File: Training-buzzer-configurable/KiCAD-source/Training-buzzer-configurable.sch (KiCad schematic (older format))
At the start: 16 parts, among them J1 Con, J2 DC Jack 5V, Q1 BC547B, Q2 BC547B, Q3 BC547B

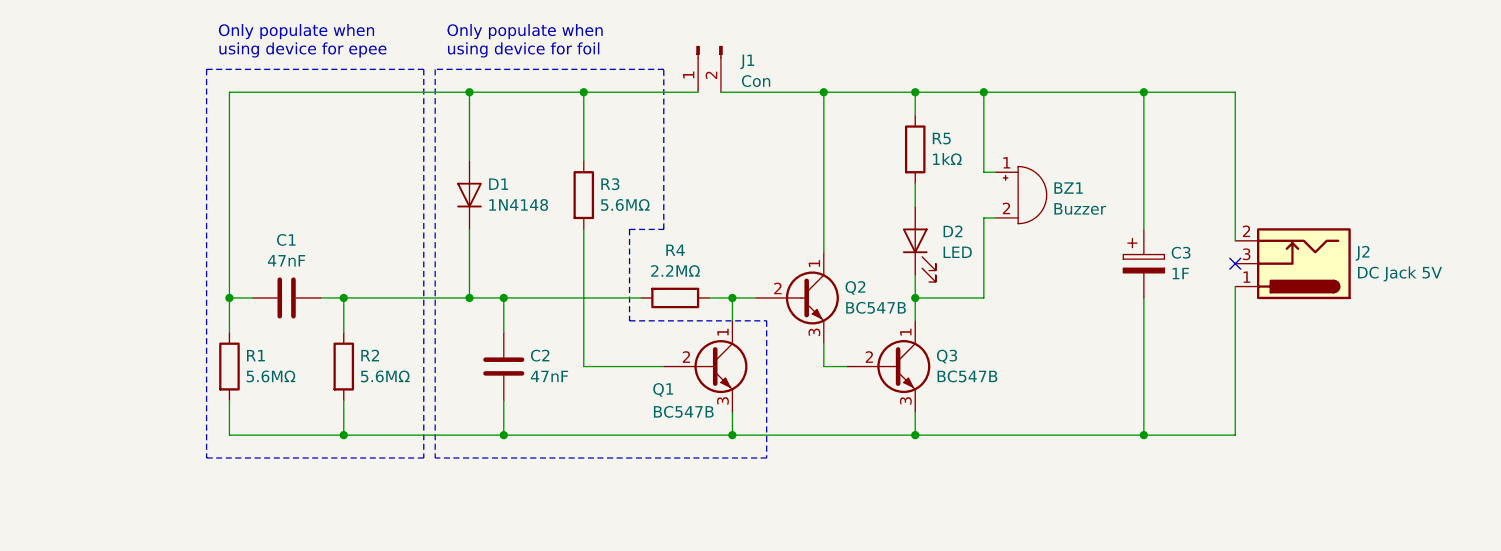
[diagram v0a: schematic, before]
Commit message: Rework circuit using NOR gates and create PCB
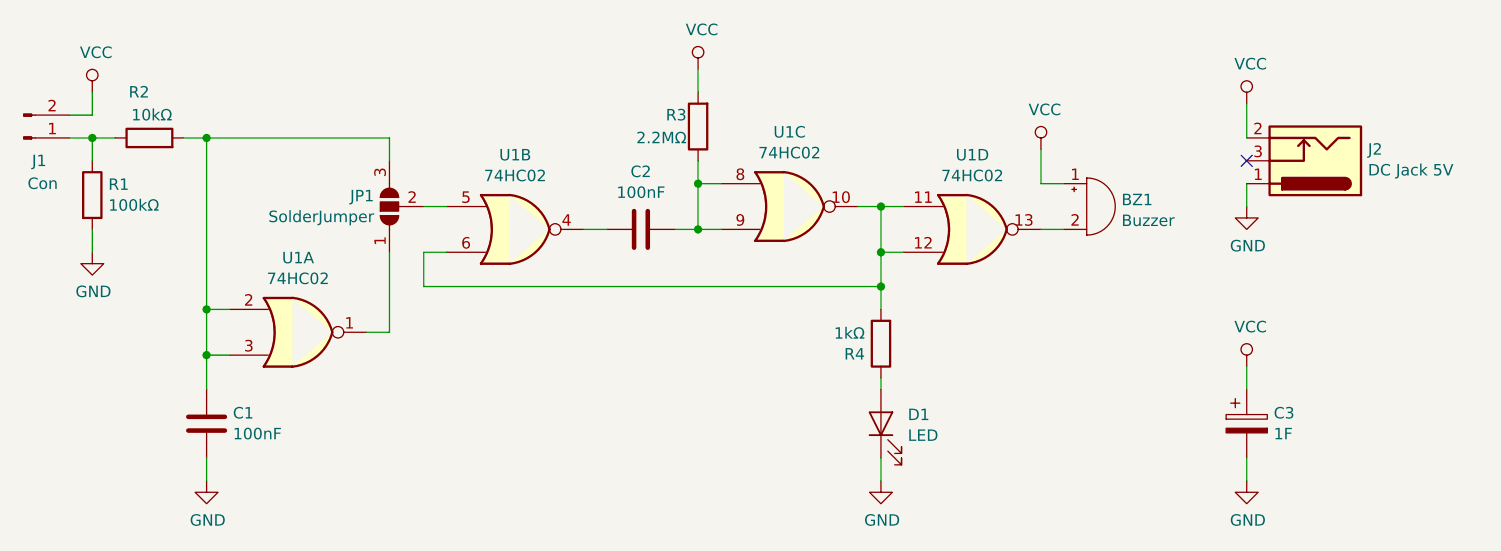
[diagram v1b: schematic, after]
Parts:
- removed D1: 1N4148, Diode_THT:D_A-405_P7.62mm_Horizontal, symbol Device:D
- removed Q1, Q2, Q3: BC547B, Package_TO_SOT_THT:TO-92_Inline, symbol Transistor_BJT:BC547
- removed R4: 2.2MΩ, Resistor_THT:R_Axial_DIN0207_L6.3mm_D2.5mm_P10.16mm_Horizontal, symbol Device:R
- added JP1: SolderJumper, Jumper:SolderJumper-3_P1.3mm_Open_RoundedPad1.0x1.5mm, symbol Jumper:SolderJumper_3_Open
- added U1: 74HC02, Package_DIP:DIP-14_W7.62mm_LongPads, symbol 74xx:74HC02
- C1, C2: value 47nF -> 100nF; footprint Capacitor_THT:C_Disc_D5.0mm_W2.5mm_P2.50mm -> Capacitor_THT:C_Disc_D4.3mm_W1.9mm_P5.00mm
- R1: value 5.6MΩ -> 100kΩ
- R2: value 5.6MΩ -> 10kΩ
- R3: value 5.6MΩ -> 2.2MΩ
- renumbered D2 to D1, R5 to R4
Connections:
- net GND: now reaches C3.2, J2.1, R1.2
- net GND: now also C1.1, D1.1 (K); no longer C2.2, R2.2
- net VCC: now reaches BZ1.1 (-), C3.1, J1.2 (Pin_2), J2.2
- net VCC: now also R3.2; no longer R4.1
- net at BZ1.2 (+): now also U1.13; no longer D1.1 (K)
- net at D1.2 (A): now also R4.1; no longer R4.2
- net at J1.1 (Pin_1), R1.1: now also R2.1; no longer C1.2, R3.1
- new net: R4.2, U1.10, U1.11, U1.12, U1.6
- new net: C2.1, R3.1, U1.8, U1.9
- new net: C2.2, U1.4
- new net: JP1.2 (C), U1.5
- new net: JP1.1 (A), U1.1
- new net: C1.2, JP1.3 (B), R2.2, U1.2, U1.3
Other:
- note removed: "Only populate when \nusing device for epee"
- note removed: "Only populate when\nusing device for foil\n"
- moved on the sheet: BZ1, C3, D1, J1, J2, R4
